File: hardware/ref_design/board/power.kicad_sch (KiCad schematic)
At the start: 23 parts, among them Q1 2N7002, SW17 PWR, U3 TPS63001DRCR

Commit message: Reference design: case, board pipeline, routing tools and docs
- case/case.scad now owns every position the board needs (outline,
  cable slot, contacts, screws, USB-C, power button, pinholes, light
  pipes, height limits) and exports them to positions.json; tub, lid
  and power cap STLs, lens and board outlines as DXF.
- board/placement.py + tools/build_pcb.py: a 4-layer board built from
  KiCad's netlist with pcbnew, every footprint linked to its symbol
  (DRC schematic parity: 0), the RP2350B core's placement, routing and
  regulator copper copied from Raspberry Pi's minimal design.
- tools/route.py: planes, pre-routes the autorouter can't do (membrane
  combs, the display's grounded RGB pins, plane fan-out), Freerouting
  1.9 on a corrected copy of the board, pours, stitching, repair.
- Footprint copies that carry vendor 3D models (USB-C, JST, switches)
  checked against their pads; speaker pads moved to the back as SMD;
  the Alps switch's pads pulled back from its locating holes.
- docs: README, assembly, bring-up, pin map (generated), BOM, design
  review, and the Konnect problems met on the way.

Co-Authored-By: Claude Opus 5.5 (1M context) <noreply@anthropic.com>
Claude-Session: https://claude.ai/code/session_01KGgEu3CbFtCsvHRQgAFiCN
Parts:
- SW17: footprint Button_Switch_SMD:SW_Push_1P1T-MP_NO_Horizontal_Alps_SKRTLAE010 -> battler:SW_Alps_SKRTLAE010_Pullback
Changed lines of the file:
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@@
         (font
           (size 1.27 1.27))))
-    (property "Footprint" "Button_Switch_SMD:SW_Push_1P1T-MP_NO_Horizontal_Alps_SKRTLAE010"
+    (property "Footprint" "battler:SW_Alps_SKRTLAE010_Pullback"
       (at 40.64 91.44 0)
       (effects

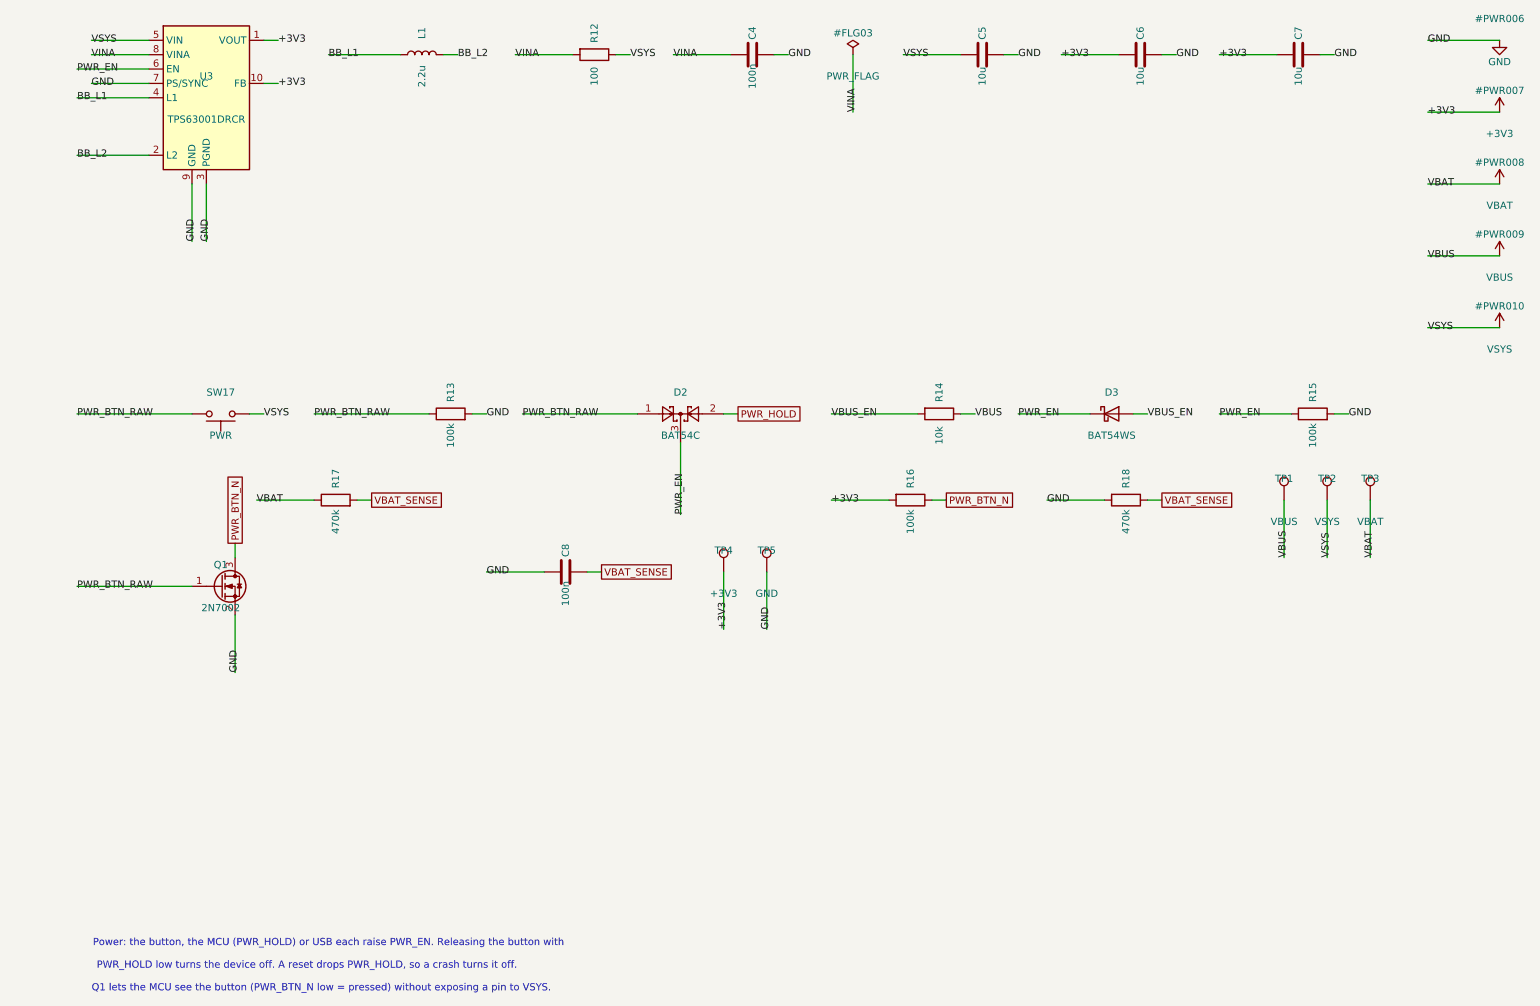
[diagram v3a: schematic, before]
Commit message: 2-layer fork: approved circuit changes in the design data and schematic
TP4056 charger (500 mA, TEMP grounded) with USB load sharing (B5819W, AO3401A
gate fed through a BAT54WS so it switches at once on an unplug, 22 uF on VSYS),
ME6211 3V3 LDO on the power latch, RP2354B with its flash inside (only the
QSPI_SS strap outside), 27 ohm 0603 USB resistors, SRV05-4 ESD, PWM audio
through two RC poles into an FM8002A, seat 1's Y contact as the power button,
no LEDs, no thermistor. Thermal-via footprints use 0.3 mm holes. Netlist
check passes, ERC 0 errors.

Co-Authored-By: Claude Opus 5.5 <noreply@anthropic.com>
Claude-Session: https://claude.ai/code/session_01KGgEu3CbFtCsvHRQgAFiCN
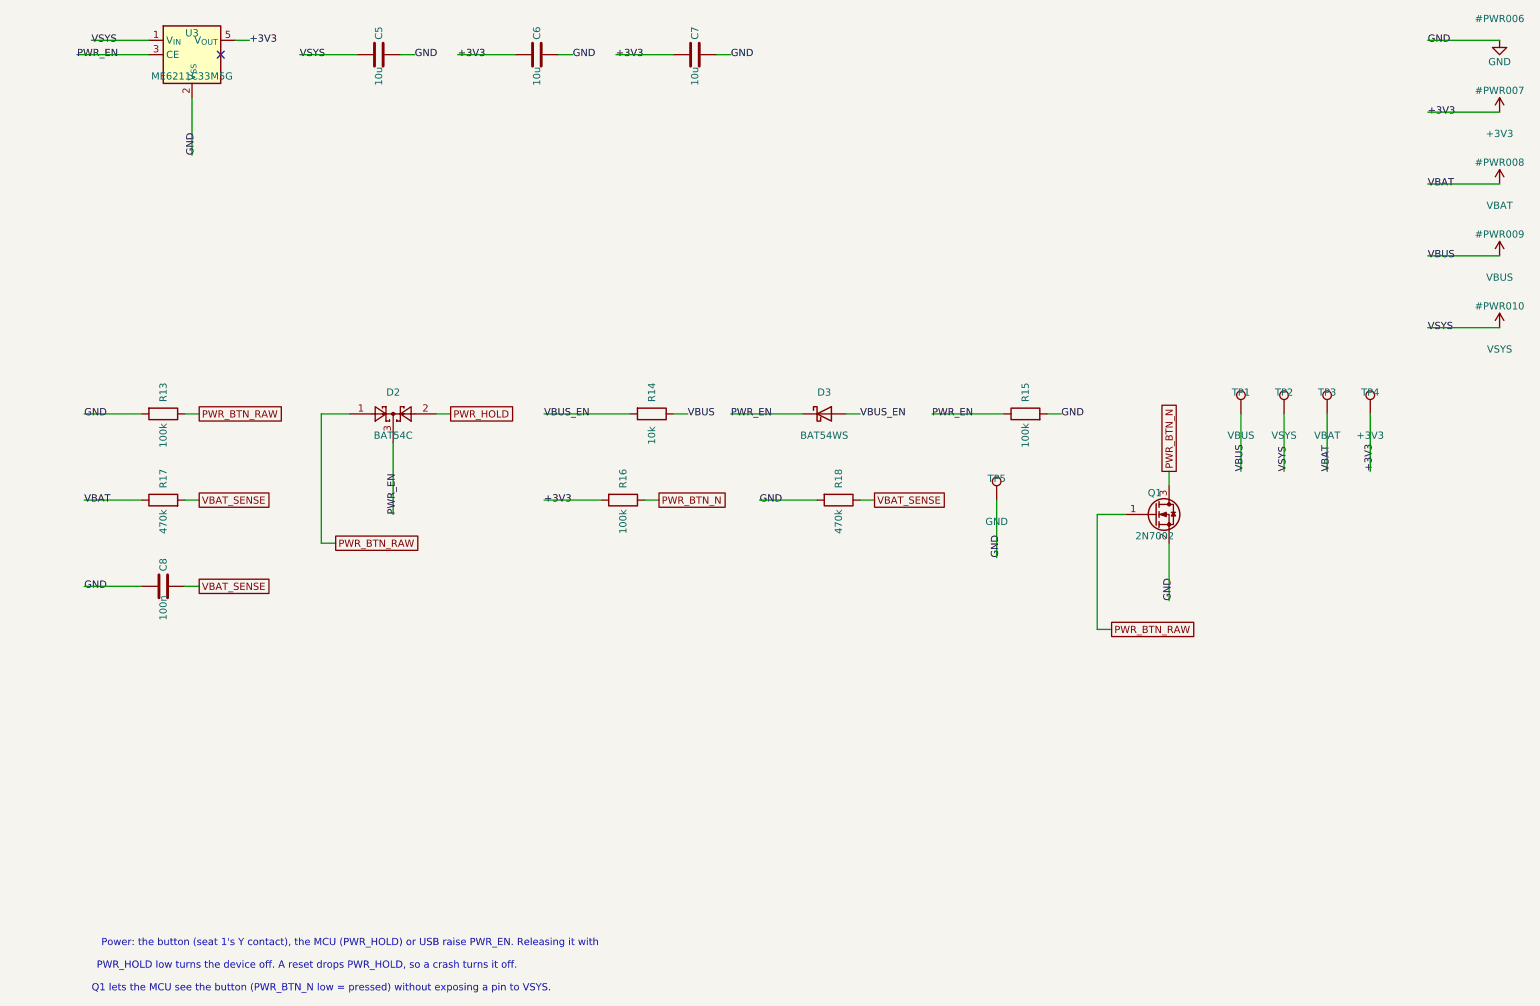
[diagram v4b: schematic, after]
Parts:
- removed C4: 100n, Capacitor_SMD:C_0402_1005Metric, symbol Device:C
- removed L1: 2.2u, Inductor_SMD:L_1008_2520Metric, symbol Device:L
- removed R12: 100, Resistor_SMD:R_0402_1005Metric, symbol Device:R
- removed SW17: PWR, battler:SW_Alps_SKRTLAE010_Pullback, symbol Switch:SW_Push
- removed U3: TPS63001DRCR, Package_SON:Texas_DRC0010J_ThermalVias, symbol Regulator_Switching:TPS63000
- added U3: ME6211C33M5G, Package_TO_SOT_SMD:SOT-23-5, symbol Regulator_Linear:ME6211C33M5
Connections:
- net +3V3: now also U3.5 (V_{OUT})
- net GND: now also U3.2 (V_{SS})
- net PWR_EN: now also U3.3 (CE)
- net VSYS: now also U3.1 (V_{IN})
- no-connect marks 0 -> 1
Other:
- note added: "Power: the button (seat 1's Y contact), the MCU (PWR_HOLD) or USB raise PWR_EN. Releasing it with"
- note removed: "Power: the button, the MCU (PWR_HOLD) or USB each raise PWR_EN. Releasing the button with"

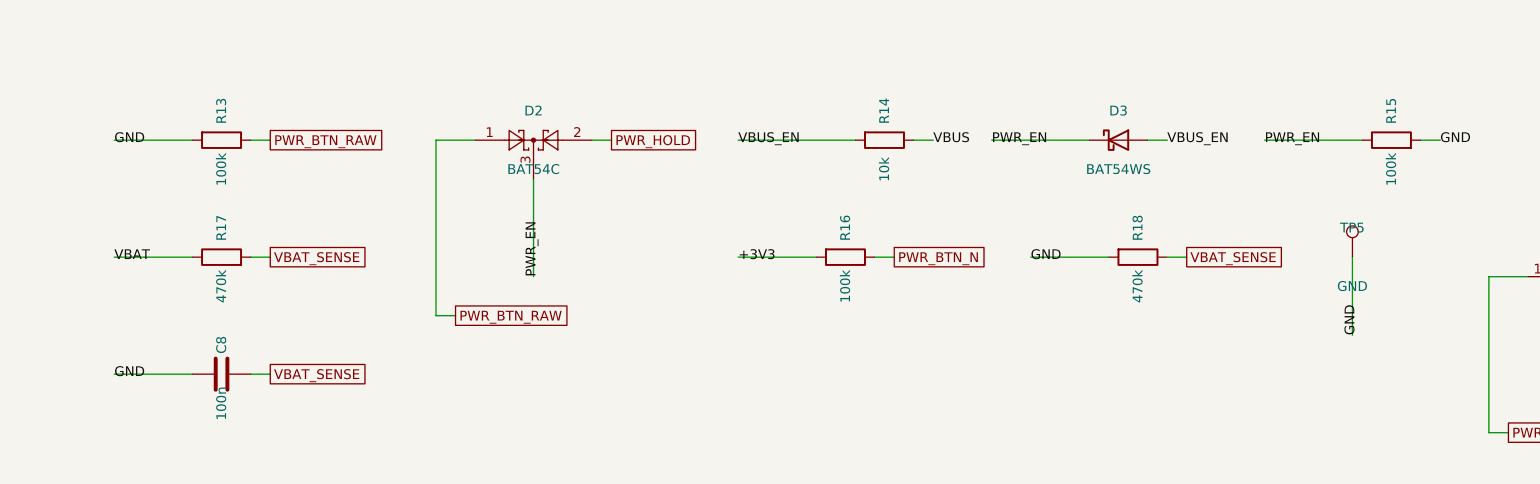
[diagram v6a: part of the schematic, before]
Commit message: Reference design: audit round 1 fixes (USB ESD reference, PWR_EN pull-down)
From an independent audit of the 2-layer board:
- SRV05-4 REF (U1 pin 5) moves from VBUS to 3V3. On VBUS, with no cable in,
  the MCU's D+ pull-up (always on in BOOTSEL mode) fed VBUS through the D+
  steering diode to about 2.7 V: PWR_EN stayed up, so the device could not
  turn off, and the load-sharing FET was left half on.
- R15 (PWR_EN pull-down) 100k -> 10k, so D5's reverse leakage into the VBUS
  node can't lift the ME6211's CE to 1.0 V when warm.
- J6 (UART) turned 180 degrees: its mouth faced J5's back 5 mm away.
- Lid: the panel's locating frame gets 0.8 mm clearance (panel_fit), not 0.4.
- Docs: ILI9488 reads at 5 MHz or less, TP4056 current 460-500 mA and its
  145 C thermal limit, how 3V3 reaches the core pour, FPC insertion depth and
  expected slack, JLC's 374 solder joints, board size as quoted.

Checks: netlist PASS, ERC 0, DRC 0 errors / 0 unconnected / 0 parity
(2 cosmetic silk warnings), fit PASS on 91 parts.

Co-Authored-By: Claude Opus 5.5 <noreply@anthropic.com>
Claude-Session: https://claude.ai/code/session_01KGgEu3CbFtCsvHRQgAFiCN
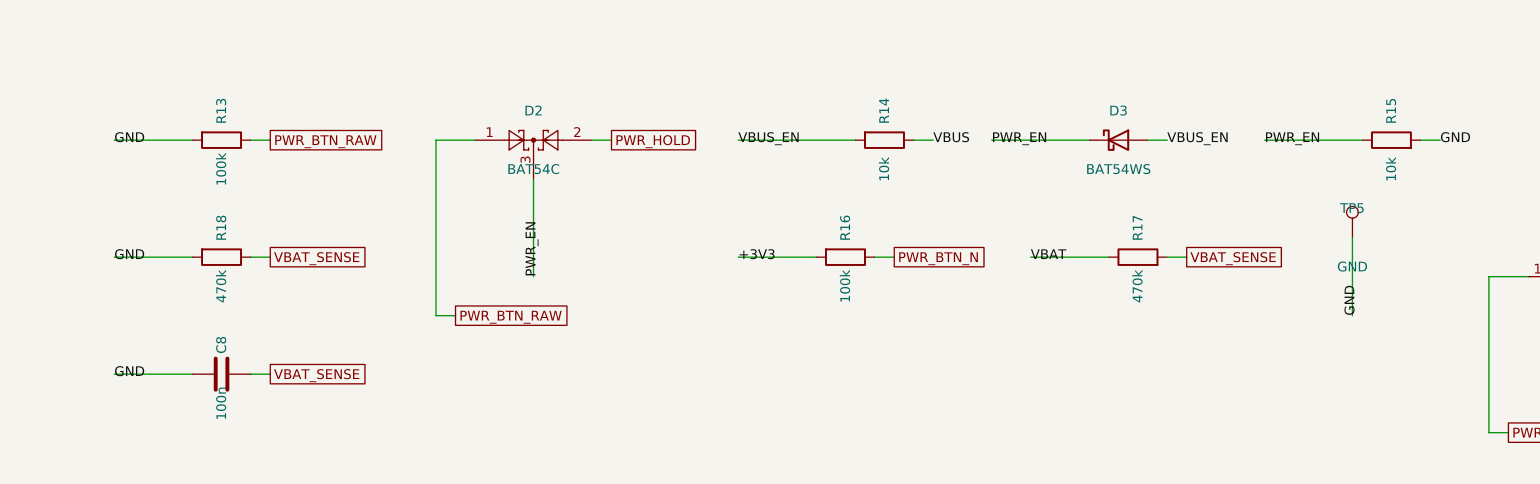
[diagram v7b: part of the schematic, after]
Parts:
- R15: value 100k -> 10k; LCSC C25741 -> C25744; MPN 0402WGF1003TCE -> 0402WGF1002TCE
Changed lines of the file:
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@@
+  (wire
+    (pts
+      (xy 146.05 106.68)
+      (xy 135.89 106.68))
+)
+  (wire
+    (pts
+      (xy 153.67 106.68)
+      (xy 156.21 106.68))
+)
+  (wire
+    (pts
+      (xy 34.29 106.68)
+      (xy 36.83 106.68))
+)
   (wire
     (pts
@@
   (wire
     (pts
-      (xy 34.29 106.68)
-      (xy 36.83 106.68))
-)
-  (wire
-    (pts
-      (xy 153.67 106.68)
-      (xy 156.21 106.68))
-)
-  (wire
-    (pts
-      (xy 146.05 106.68)
-      (xy 135.89 106.68))
-)
-  (wire
-    (pts
       (xy 34.29 121.92)
       (xy 36.83 121.92))
@@
   (wire
     (pts
-      (xy 177.8 106.68)
-      (xy 177.8 116.84))
+      (xy 177.8 104.14)
+      (xy 177.8 114.3))
 )
   (wire
@@
 )
   (label "VBAT"
+    (at 135.89 106.68 0)
+)
+  (label "GND"
     (at 16.51 106.68 0)
-)
-  (label "GND"
-    (at 135.89 106.68 0)
 )
   (label "GND"
@@
 )
   (label "GND"
-    (at 177.8 116.84 90)
+    (at 177.8 114.3 90)
 )
   (label "GND"
@@
   (global_label "VBAT_SENSE"
     (shape passive)
-    (at 36.83 106.68 0)
+    (at 156.21 106.68 0)
 )
   (global_label "VBAT_SENSE"
     (shape passive)
-    (at 156.21 106.68 0)
+    (at 36.83 106.68 0)
 )
   (global_label "VBAT_SENSE"
@@
         (font
           (size 1.27 1.27))))
-    (property "Value" "100k"
+    (property "Value" "10k"
       (at 182.88 95.25 0)
       (effects
@@
           (size 1.27 1.27))
         (hide yes)))
-    (property "LCSC" "C25741"
-      (at 0 0 0)
-      (effects
-        (font
-          (size 1.27 1.27))
-        (hide yes)))
-    (property "MPN" "0402WGF1003TCE"
+    (property "LCSC" "C25744"
+      (at 0 0 0)
+      (effects
+        (font
+          (size 1.27 1.27))
+        (hide yes)))
+    (property "MPN" "0402WGF1002TCE"
       (at 0 0 0)
       (effects
@@
   (symbol
     (lib_id "Device:R")
-    (at 30.48 106.68 90)
+    (at 149.86 106.68 90)
     (unit 1)
     (in_bom yes)
@@
     (dnp no)
     (property "Reference" "R17"
+      (at 149.86 102.87 0)
+      (effects
+        (font
+          (size 1.27 1.27))))
+    (property "Value" "470k"
+      (at 149.86 110.49 0)
+      (effects
+        (font
+          (size 1.27 1.27))))
+    (property "Footprint" "Resistor_SMD:R_0402_1005Metric"
+      (at 149.86 106.68 0)
+      (effects
+        (font
+          (size 1.27 1.27))
+        (hide yes)))
+    (property "Datasheet" ""
+      (at 149.86 106.68 0)
+      (effects
+        (font
+          (size 1.27 1.27))
+        (hide yes)))
+    (property "LCSC" "C25790"
+      (at 0 0 0)
+      (effects
+        (font
+          (size 1.27 1.27))
+        (hide yes)))
+    (property "MPN" "0402WGF4703TCE"
+      (at 0 0 0)
+      (effects
+        (font
+          (size 1.27 1.27))
+        (hide yes)))
+    (property "Manufacturer" "UNI-ROYAL"
+      (at 0 0 0)
+      (effects
+        (font
+          (size 1.27 1.27))
+        (hide yes)))
+    (instances
+      (project ""
+        (path "/"
+          (reference "R17")
+          (unit 1)))))
+  (symbol
+    (lib_id "Device:R")
+    (at 30.48 106.68 270)
+    (unit 1)
+    (in_bom yes)
+    (on_board yes)
+    (dnp no)
+    (property "Reference" "R18"
       (at 30.48 102.87 0)
       (effects
@@
       (project ""
         (path "/"
-          (reference "R17")
-          (unit 1)))))
-  (symbol
-    (lib_id "Device:R")
-    (at 149.86 106.68 270)
-    (unit 1)
-    (in_bom yes)
-    (on_board yes)
-    (dnp no)
-    (property "Reference" "R18"
-      (at 149.86 102.87 0)
-      (effects
-        (font
-          (size 1.27 1.27))))
-    (property "Value" "470k"
-      (at 149.86 110.49 0)
-      (effects
-        (font
-          (size 1.27 1.27))))
-    (property "Footprint" "Resistor_SMD:R_0402_1005Metric"
-      (at 149.86 106.68 0)
-      (effects
-        (font
-          (size 1.27 1.27))
-        (hide yes)))
-    (property "Datasheet" ""
-      (at 149.86 106.68 0)
-      (effects
-        (font
-          (size 1.27 1.27))
-        (hide yes)))
-    (property "LCSC" "C25790"
-      (at 0 0 0)
-      (effects
-        (font
-          (size 1.27 1.27))
-        (hide yes)))
-    (property "MPN" "0402WGF4703TCE"
-      (at 0 0 0)
-      (effects
-        (font
-          (size 1.27 1.27))
-        (hide yes)))
-    (property "Manufacturer" "UNI-ROYAL"
-      (at 0 0 0)
-      (effects
-        (font
-          (size 1.27 1.27))
-        (hide yes)))
-    (instances
-      (project ""
-        (path "/"
           (reference "R18")
           (unit 1)))))
@@
   (symbol
     (lib_id "Connector:TestPoint")
-    (at 177.8 106.68 0)
+    (at 177.8 104.14 0)
     (unit 1)
     (in_bom yes)
@@
     (dnp no)
     (property "Reference" "TP5"
-      (at 177.8 102.87 0)
+      (at 177.8 100.33 0)
       (effects
         (font
           (size 1.27 1.27))))
     (property "Value" "GND"
-      (at 177.8 110.49 0)
+      (at 177.8 107.95 0)
       (effects
         (font
           (size 1.27 1.27))))
     (property "Footprint" "TestPoint:TestPoint_Pad_D1.0mm"
-      (at 177.8 106.68 0)
-      (effects
-        (font
-          (size 1.27 1.27))
-        (hide yes)))
-    (property "Datasheet" ""
-      (at 177.8 106.68 0)
-      (effects
-        (font
+      (at 177.8 104.14 0)
+      (effects
+        (font
+          (size 1.27 1.27))
+        (hide yes)))
+    (property "Datasheet" ""
+      (at 177.8 104.14 0)
+      (effects
+        (font
